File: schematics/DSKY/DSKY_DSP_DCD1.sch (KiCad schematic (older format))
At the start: 11 parts, among them U17 74LS32, U18 74LS00, U19 74LS04, U42 74LS04, U43 74LS00, U48 74LS00, U51 74LS244, U52 74LS244, U60 74LS10, U61 74LS244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

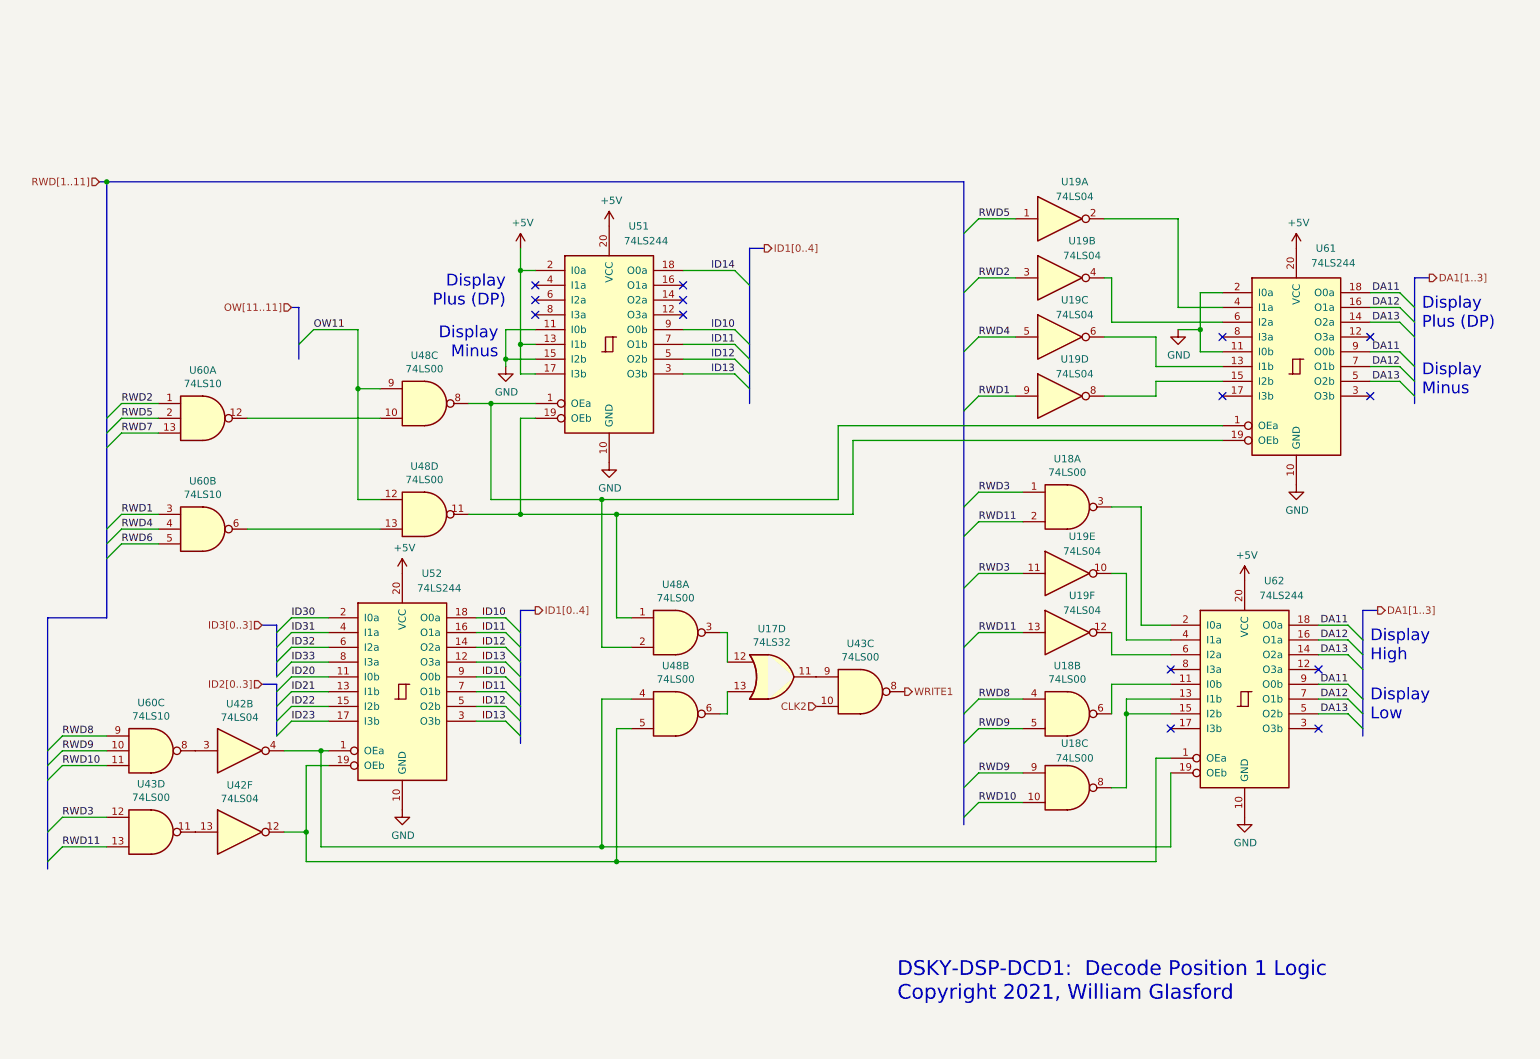
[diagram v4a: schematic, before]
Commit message: Sign processing overhauled.
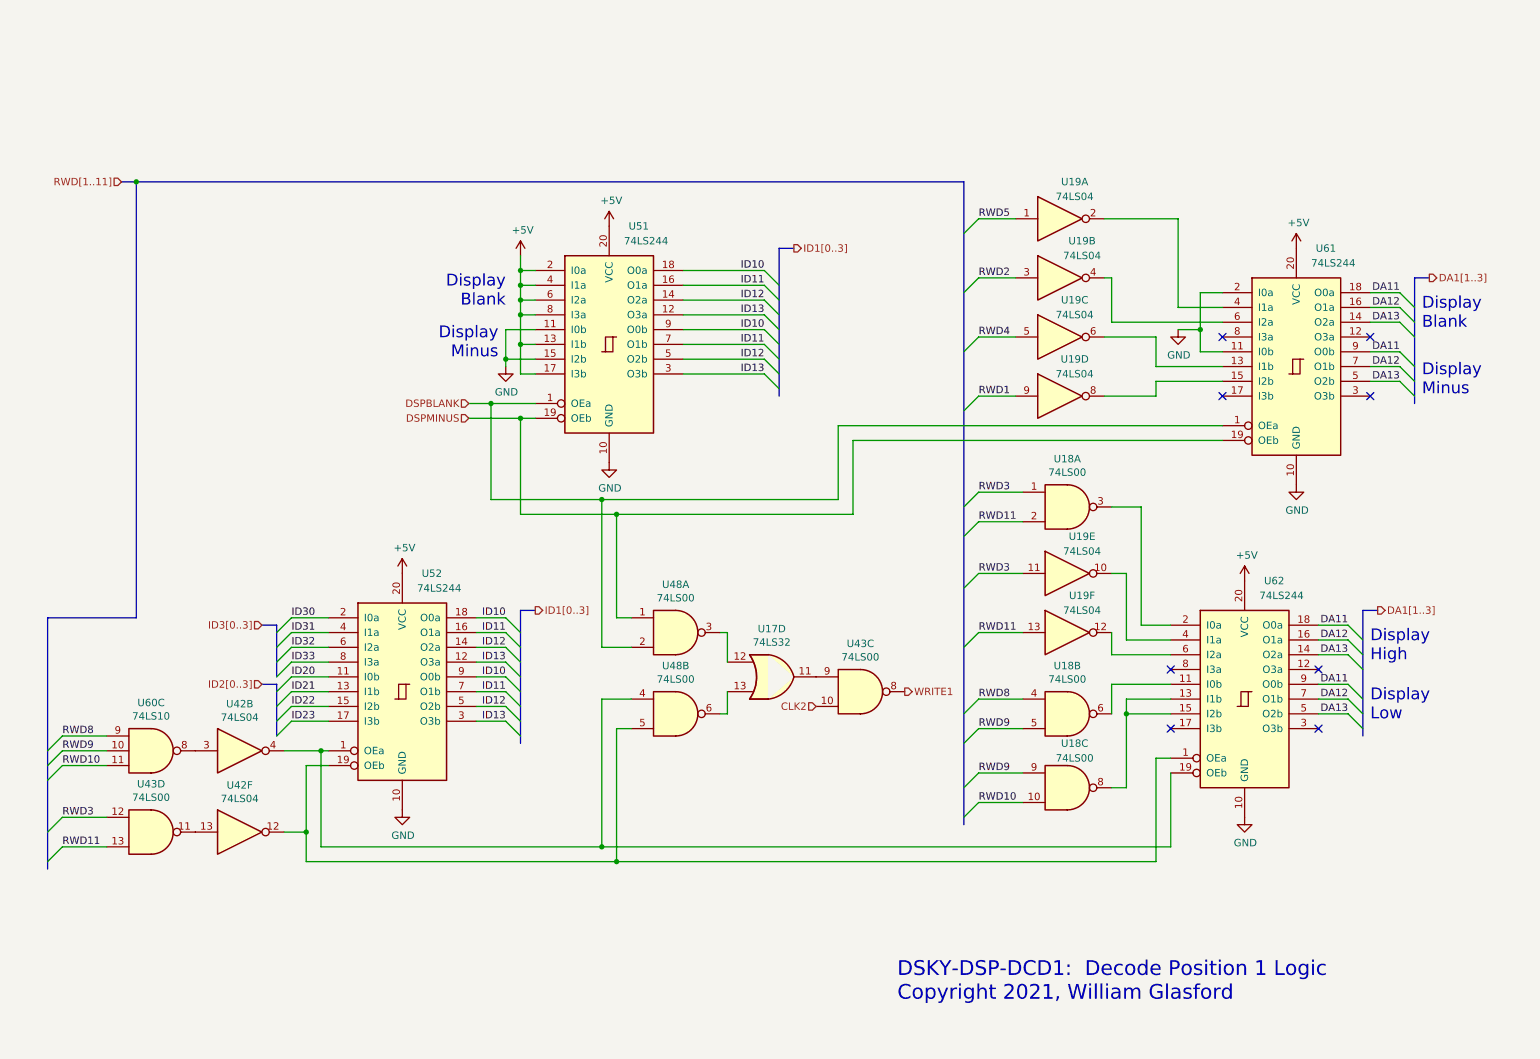
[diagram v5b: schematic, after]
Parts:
- removed unit 4 of U48
- removed unit 3 of U48
- removed unit 1 of U60
- removed unit 2 of U60
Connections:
- net ID14 is gone; now on net ID10: U51.18 (O0a)
- net +5V: now also U51.4 (I1a), U51.6 (I2a), U51.8 (I3a)
- net ID11: now also U51.16 (O1a)
- net ID12: now also U51.14 (O2a)
- net ID13: now also U51.12 (O3a)
- net DSPMINUS: now reaches U48.1, U51.19 (OEb), U61.19 (OEb)
- net DSPBLANK: now reaches U48.2, U51.1 (OEa), U61.1 (OEa)
- no-connect marks 14 -> 8
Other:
- note added: "Display\nBlank"
- note removed: "Display\nPlus (DP)"
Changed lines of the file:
@@
 $Descr A 11000 8500
 encoding utf-8
-Sheet 6 10
+Sheet 8 11
 Title ""
 Date ""
@@
 Wire Wire Line
 	1000 6200 700  6200
-Wire Wire Line
-	1350 3950 1100 3950
-Wire Wire Line
-	1350 4050 1100 4050
-Wire Wire Line
-	1350 4150 1100 4150
-Entry Wire Line
-	1000 4050 1100 3950
-Entry Wire Line
-	1000 4150 1100 4050
-Entry Wire Line
-	1000 4250 1100 4150
 Entry Wire Line
 	600  5550 700  5450
@@
 Entry Wire Line
 	600  6300 700  6200
-Text Label 1100 3950 0    50   ~ 0
-RWD1
-Text Label 1100 4050 0    50   ~ 0
-RWD4
-Text Label 1100 4150 0    50   ~ 0
-RWD6
 Text Label 700  5450 0    50   ~ 0
 RWD8
@@
 Text Label 700  5650 0    50   ~ 0
 RWD10
-Text HLabel 950  1700 0    50   Input ~ 0
+Text HLabel 1100 1700 0    50   Input ~ 0
 RWD[1..11]
 Wire Wire Line
@@
 Wire Wire Line
 	8200 5700 8200 6200
-Wire Bus Line
-	950  1700 1000 1700
 Text Notes 6350 7250 0    100  ~ 0
 DSKY-DSP-DCD1:  Decode Position 1 Logic\nCopyright 2021, William Glasford
@@
 Wire Wire Line
 	7900 5300 8200 5300
-Wire Wire Line
-	1350 3200 1100 3200
-Wire Wire Line
-	1350 3300 1100 3300
-Wire Wire Line
-	1350 3400 1100 3400
-Entry Wire Line
-	1000 3300 1100 3200
-Entry Wire Line
-	1000 3400 1100 3300
-Entry Wire Line
-	1000 3500 1100 3400
-Text Label 1100 3200 0    50   ~ 0
-RWD2
-Text Label 1100 3300 0    50   ~ 0
-RWD5
-Text Label 1100 3400 0    50   ~ 0
-RWD7
 Text Notes 9900 3150 0    80   ~ 0
 Display\nMinus
@@
 Display\nHigh
 Text Notes 9900 2700 0    80   ~ 0
-Display\nPlus (DP)
+Display\nBlank
 Wire Wire Line
 	8250 2550 8550 2550
@@
 	1    0    0    -1
 $EndComp
-Entry Wire Line
-	2300 2800 2400 2700
-Text Label 2400 2700 0    50   ~ 0
-OW11
-Text HLabel 2250 2550 0    50   Input ~ 0
-OW[11..11]
-Wire Wire Line
-	2400 2700 2700 2700
-Wire Wire Line
-	2850 4050 1950 4050
-$Comp
-L 74xx:74LS00 U48
-U 3 1 62581BC9
-P 3150 3200
-F 0 "U48" H 3150 3525 50  0000 C CNN
-F 1 "74LS00" H 3150 3434 50  0000 C CNN
-F 2 "" H 3150 3200 50  0001 C CNN
-F 3 "http://www.ti.com/lit/gpn/sn74ls00" H 3150 3200 50  0001 C CNN
-	3    3150 3200
-	1    0    0    -1
-$EndComp
-$Comp
-L 74xx:74LS00 U48
-U 4 1 624DAC9B
-P 3150 3950
-F 0 "U48" H 3150 4275 50  0000 C CNN
-F 1 "74LS00" H 3150 4184 50  0000 C CNN
-F 2 "" H 3150 3950 50  0001 C CNN
-F 3 "http://www.ti.com/lit/gpn/sn74ls00" H 3150 3950 50  0001 C CNN
-	4    3150 3950
-	1    0    0    -1
-$EndComp
 Wire Wire Line
 	2200 6100 2350 6100
@@
 Connection ~ 3600 3200
 Wire Wire Line
-	3600 3200 3600 3850
-Connection ~ 3800 3950
-Wire Wire Line
-	3450 3950 3800 3950
-Text Label 5250 2300 2    50   ~ 0
-ID14
-Entry Wire Line
-	5250 2300 5350 2400
-Wire Wire Line
-	4900 2300 5250 2300
-Wire Wire Line
-	3800 2300 3800 2150
-Connection ~ 3800 2300
+	3450 3300 3800 3300
+Text Label 5450 2300 2    50   ~ 0
+ID10
+Entry Wire Line
+	5450 2300 5550 2400
+Wire Wire Line
+	4900 2300 5450 2300
 Wire Wire Line
 	3900 2300 3800 2300
@@
 Wire Wire Line
 	3450 3200 3600 3200
-NoConn ~ 3900 2600
-NoConn ~ 3900 2500
-NoConn ~ 3900 2400
-NoConn ~ 4900 2600
-NoConn ~ 4900 2500
-NoConn ~ 4900 2400
 $Comp
 L 74xx:74LS244 U?
@@
 	1    0    0    -1
 $EndComp
-Wire Wire Line
-	3800 2800 3800 2300
-Connection ~ 3800 2800
-Text Label 5250 3000 2    50   ~ 0
+Text Label 5450 3000 2    50   ~ 0
 ID13
 Wire Wire Line
 	4450 5400 4450 6300
 Text Notes 3700 2550 2    80   ~ 0
-Display\nPlus (DP)
+Display\nBlank
 Wire Wire Line
 	2450 5550 2200 5550
@@
 	3700 5150 3800 5250
 Text HLabel 3900 4600 2    50   Output ~ 0
-ID1[0..4]
+ID1[0..3]
 Text Label 3700 5350 2    50   ~ 0
 ID13
@@
 	1    0    0    -1
 $EndComp
-Text Label 5250 2900 2    50   ~ 0
+Text Label 5450 2900 2    50   ~ 0
 ID12
-Text Label 5250 2800 2    50   ~ 0
+Text Label 5450 2800 2    50   ~ 0
 ID11
-Text Label 5250 2700 2    50   ~ 0
+Text Label 5450 2700 2    50   ~ 0
 ID10
 Entry Wire Line
-	5250 3000 5350 3100
-Entry Wire Line
-	5250 2900 5350 3000
-Entry Wire Line
-	5250 2800 5350 2900
-Entry Wire Line
-	5250 2700 5350 2800
-Wire Wire Line
-	4900 2800 5250 2800
-Wire Wire Line
-	4900 2700 5250 2700
-Wire Wire Line
-	4900 3000 5250 3000
-Wire Wire Line
-	4900 2900 5250 2900
+	5450 3000 5550 3100
+Entry Wire Line
+	5450 2900 5550 3000
+Entry Wire Line
+	5450 2800 5550 2900
+Entry Wire Line
+	5450 2700 5550 2800
+Wire Wire Line
+	4900 2800 5450 2800
+Wire Wire Line
+	4900 2700 5450 2700
+Wire Wire Line
+	4900 3000 5450 3000
+Wire Wire Line
+	4900 2900 5450 2900
 $Comp
 L power:GND #PWR?
@@
 L power:+5V #PWR?
 U 1 1 66B437B9
-P 3800 2150
+P 3800 2200
 AR Path="/60F98A64/637944C1/66B437B9" Ref="#PWR?"  Part="1"
 AR Path="/60F98A64/64844A8A/66B437B9" Ref="#PWR0192"  Part="1"
-F 0 "#PWR0192" H 3800 2000 50  0001 C CNN
-F 1 "+5V" H 3815 2323 50  0000 C CNN
-F 2 "" H 3800 2150 50  0001 C CNN
-F 3 "" H 3800 2150 50  0001 C CNN
-	1    3800 2150
-	1    0    0    -1
-$EndComp
-Wire Bus Line
-	5450 2150 5350 2150
-Text HLabel 5450 2150 2    50   Output ~ 0
-ID1[0..4]
+F 0 "#PWR0192" H 3800 2050 50  0001 C CNN
+F 1 "+5V" H 3815 2373 50  0000 C CNN
+F 2 "" H 3800 2200 50  0001 C CNN
+F 3 "" H 3800 2200 50  0001 C CNN
+	1    3800 2200
+	1    0    0    -1
+$EndComp
+Wire Bus Line
+	5650 2150 5550 2150
+Text HLabel 5650 2150 2    50   Output ~ 0
+ID1[0..3]
 $Comp
 L power:+5V #PWR?
@@
 Wire Wire Line
 	4450 3950 4450 4650
-Connection ~ 1000 1700
-Wire Bus Line
-	1000 1700 6800 1700
-Wire Bus Line
-	2300 2550 2250 2550
-Wire Wire Line
-	2700 3100 2850 3100
-Wire Wire Line
-	2700 3100 2700 3850
-Wire Wire Line
-	2700 3850 2850 3850
-Connection ~ 2700 3100
-Wire Wire Line
-	2850 3300 1950 3300
-Wire Wire Line
-	2700 2700 2700 3100
 Wire Wire Line
 	5950 3350 8550 3350
@@
 	4350 6200 8200 6200
 Wire Wire Line
-	4350 3850 5950 3850
-Wire Wire Line
 	4450 3950 6050 3950
 $Comp
@@
 $Comp
 L 74xx:74LS10 U60
-U 1 1 63A57FF4
-P 1650 3300
-F 0 "U60" H 1650 3625 50  0000 C CNN
-F 1 "74LS10" H 1650 3534 50  0000 C CNN
-F 2 "" H 1650 3300 50  0001 C CNN
-F 3 "http://www.ti.com/lit/gpn/sn74LS10" H 1650 3300 50  0001 C CNN
-	1    1650 3300
-	1    0    0    -1
-$EndComp
-$Comp
-L 74xx:74LS10 U60
-U 2 1 63A59D22
-P 1650 4050
-F 0 "U60" H 1650 4375 50  0000 C CNN
-F 1 "74LS10" H 1650 4284 50  0000 C CNN
-F 2 "" H 1650 4050 50  0001 C CNN
-F 3 "http://www.ti.com/lit/gpn/sn74LS10" H 1650 4050 50  0001 C CNN
-	2    1650 4050
-	1    0    0    -1
-$EndComp
-$Comp
-L 74xx:74LS10 U60
 U 3 1 63A5CF99
 P 1300 5550
@@
 $EndComp
 Wire Bus Line
-	1000 4650 600  4650
+	1200 4650 600  4650
 Connection ~ 2350 6100
 Wire Wire Line
@@
 Wire Wire Line
 	7800 4900 8200 4900
-Wire Bus Line
-	2300 2550 2300 2900
+Wire Wire Line
+	3800 2800 3800 2600
+Connection ~ 3800 2800
+Connection ~ 3800 2300
+Wire Wire Line
+	3800 2300 3800 2200
+Wire Wire Line
+	3900 2400 3800 2400
+Connection ~ 3800 2400
+Wire Wire Line
+	3800 2400 3800 2300
+Wire Wire Line
+	3900 2500 3800 2500
+Connection ~ 3800 2500
+Wire Wire Line
+	3800 2500 3800 2400
+Wire Wire Line
+	3900 2600 3800 2600
+Connection ~ 3800 2600
+Wire Wire Line
+	3800 2600 3800 2500
+Text Label 5450 2400 2    50   ~ 0
+ID11
+Entry Wire Line
+	5450 2400 5550 2500
+Wire Wire Line
+	4900 2400 5450 2400
+Text Label 5450 2500 2    50   ~ 0
+ID12
+Entry Wire Line
+	5450 2500 5550 2600
+Wire Wire Line
+	4900 2500 5450 2500
+Text Label 5450 2600 2    50   ~ 0
+ID13
+Entry Wire Line
+	5450 2600 5550 2700
+Wire Wire Line
+	4900 2600 5450 2600
+Wire Wire Line
+	3600 3200 3600 3850
+Wire Bus Line
+	1200 1700 1200 4650
+Text HLabel 3450 3200 0    50   Input ~ 0
+DSPBLANK
+Text HLabel 3450 3300 0    50   Input ~ 0
+DSPMINUS
+Wire Wire Line
+	4350 3850 5950 3850
+Connection ~ 3800 3300
+Connection ~ 1200 1700
+Wire Bus Line
+	1200 1700 6800 1700
+Wire Bus Line
+	1100 1700 1200 1700
 Wire Bus Line
 	2150 4700 2150 5050
@@
 	2150 5100 2150 5450
 Wire Bus Line
-	1000 1700 1000 4650
-Wire Bus Line
 	600  4650 600  6350
 Wire Bus Line
@@
 	9500 4600 9500 5450
 Wire Bus Line
-	5350 2150 5350 3200
+	5550 2150 5550 3150
 Wire Bus Line
 	6800 1700 6800 6050

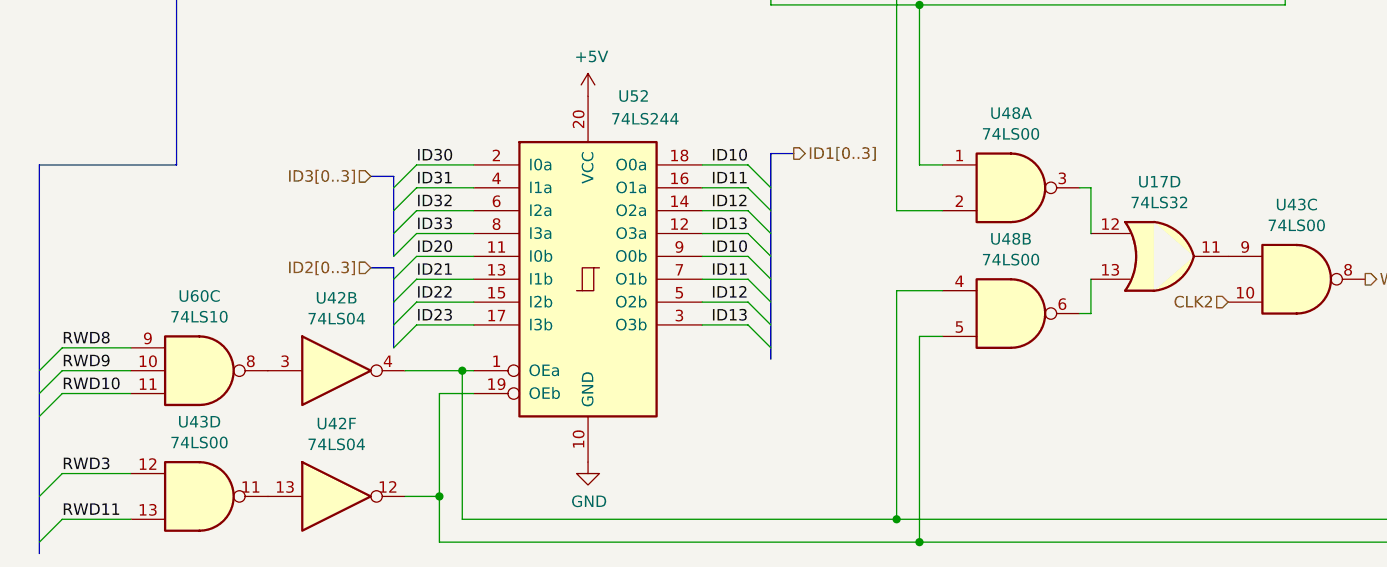
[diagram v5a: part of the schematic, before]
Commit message: Overhauled the handling of the sign characters.
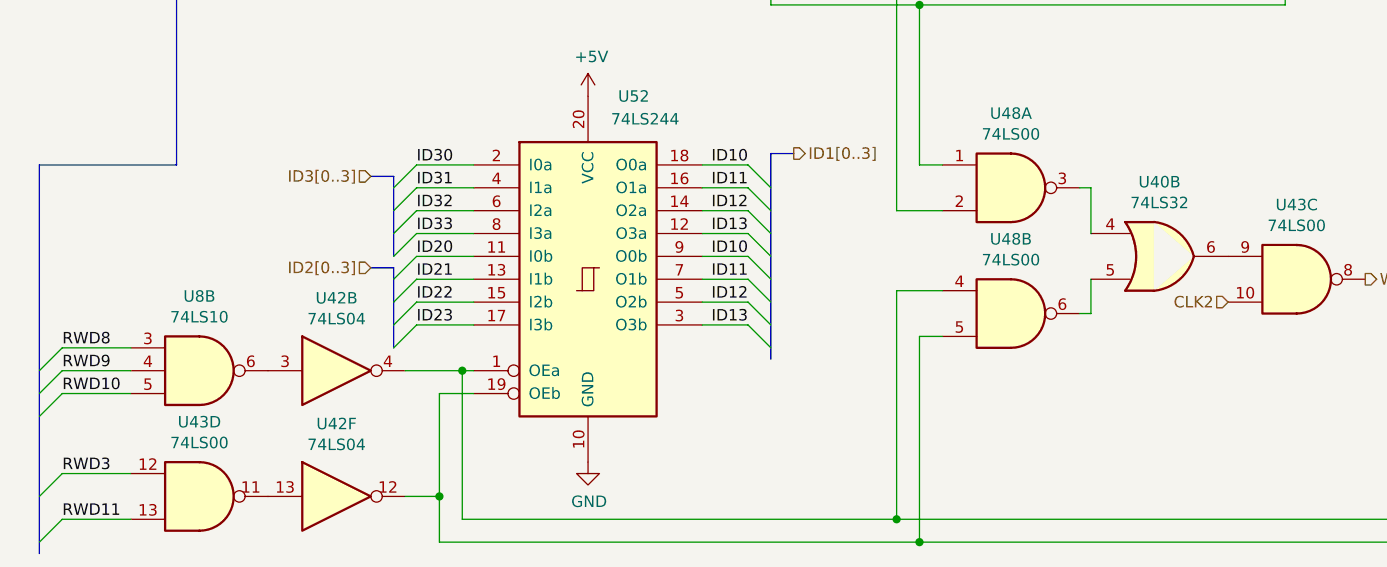
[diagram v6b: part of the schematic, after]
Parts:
- renumbered U17 to U40, U60 to U8
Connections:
- net RWD10: now also U8.5; no longer U8.11
- net RWD8: now also U8.3; no longer U8.9
- net RWD9: now also U8.4; no longer U8.10
- net at U42.3: now also U8.6; no longer U8.8
- net at U48.3: now also U40.4; no longer U40.12
- net at U48.6: now also U40.5; no longer U40.13
- net at U43.9: now also U40.6; no longer U40.11
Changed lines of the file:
@@
 	4450 3950 6050 3950
 $Comp
-L 74xx:74LS32 U17
-U 4 1 62D37341
+L 74xx:74LS32 U40
+U 2 1 62D37341
 P 5500 5050
-F 0 "U17" H 5500 5375 50  0000 C CNN
+F 0 "U40" H 5500 5375 50  0000 C CNN
 F 1 "74LS32" H 5500 5284 50  0000 C CNN
 F 2 "" H 5500 5050 50  0001 C CNN
 F 3 "http://www.ti.com/lit/gpn/sn74LS32" H 5500 5050 50  0001 C CNN
-	4    5500 5050
+	2    5500 5050
 	1    0    0    -1
 $EndComp
@@
 	2050 5100 2150 5100
 $Comp
-L 74xx:74LS10 U60
-U 3 1 63A5CF99
+L 74xx:74LS10 U8
+U 2 1 63A5CF99
 P 1300 5550
-F 0 "U60" H 1300 5875 50  0000 C CNN
+F 0 "U8" H 1300 5875 50  0000 C CNN
 F 1 "74LS10" H 1300 5784 50  0000 C CNN
 F 2 "" H 1300 5550 50  0001 C CNN
 F 3 "http://www.ti.com/lit/gpn/sn74LS10" H 1300 5550 50  0001 C CNN
-	3    1300 5550
+	2    1300 5550
 	1    0    0    -1
 $EndComp

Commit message: Minor tweaks during implementation.
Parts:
- removed unit 3 of U43
- added U58: 74LS08, symbol 74xx:74LS08
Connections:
- net CLK2: now also U58.2
- net WRITE1: now also U58.3
- net at U40.6: now also U58.1
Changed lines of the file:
@@
-	1    0    0    -1
-$EndComp
-$Comp
-L 74xx:74LS00 U43
-U 3 1 62D5D7F0
-P 6100 5150
-F 0 "U43" H 6100 5475 50  0000 C CNN
-F 1 "74LS00" H 6100 5384 50  0000 C CNN
-F 2 "" H 6100 5150 50  0001 C CNN
-F 3 "http://www.ti.com/lit/gpn/sn74ls00" H 6100 5150 50  0001 C CNN
-	3    6100 5150
 	1    0    0    -1
 $EndComp
@@
 Wire Bus Line
 	3800 4600 3800 5500
+$Comp
+L 74xx:74LS08 U58
+U 1 1 6180EAE3
+P 6100 5150
+F 0 "U58" H 6100 5475 50  0000 C CNN
+F 1 "74LS08" H 6100 5384 50  0000 C CNN
+F 2 "" H 6100 5150 50  0001 C CNN
+F 3 "http://www.ti.com/lit/gpn/sn74LS08" H 6100 5150 50  0001 C CNN
+	1    6100 5150
+	1    0    0    -1
+$EndComp
 $EndSCHEMATC

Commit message: Final tweaks, the DSKY is now complete!
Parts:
- removed unit 1 of U18
- removed unit 3 of U18
- removed unit 1 of U19
- removed unit 2 of U19
- removed unit 3 of U19
- removed unit 4 of U19
- removed U43: 74LS00, symbol 74xx:74LS00
- removed U8: 74LS10, symbol 74xx:74LS10
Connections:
- net COMB-B: now reaches U42.13
- net COMB-B: now also U62.2 (I0a)
- net COMB-A: now reaches U42.3
- net COMB-C: now reaches U62.13 (I1b), U62.15 (I2b)
- net NRWD5: now reaches U61.4 (I1a)
- net NRWD2: now reaches U61.6 (I2a)
- net NRWD4: now reaches U61.13 (I1b)
- net NRWD1: now reaches U61.15 (I2b)
- net CLK2 renamed CLK3
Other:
- moved on the sheet: U42B, U42F
